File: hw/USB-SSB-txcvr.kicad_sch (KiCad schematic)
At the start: 0 parts

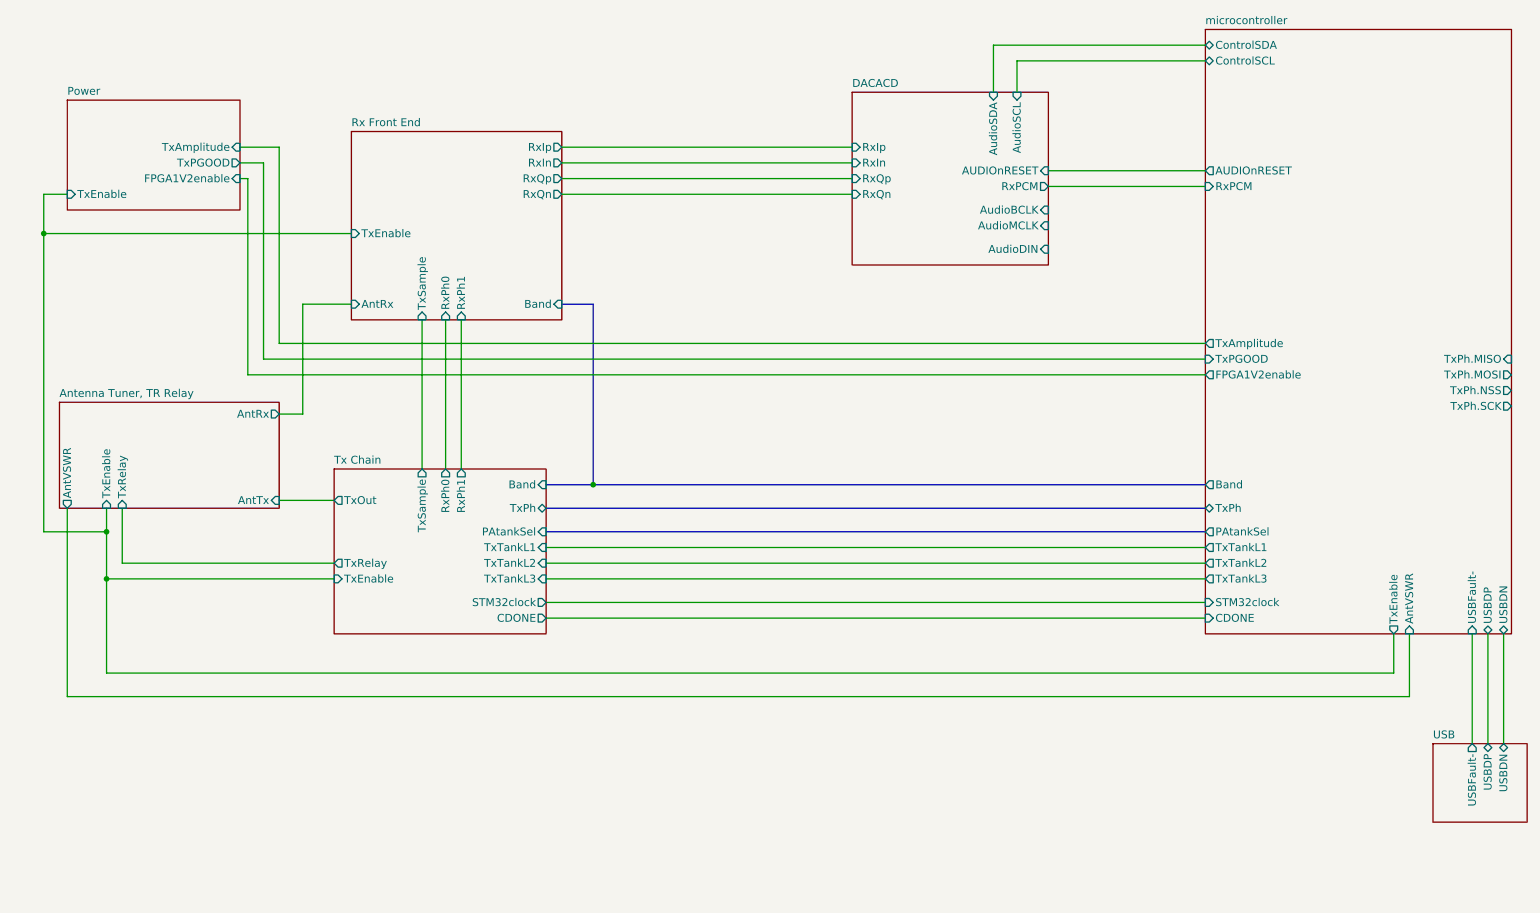
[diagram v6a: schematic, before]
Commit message: Embarking on a whole new arch for rx without BPFs and using a single digitally tuned tank plus three QSDs to accomplish image rejection in digital domain
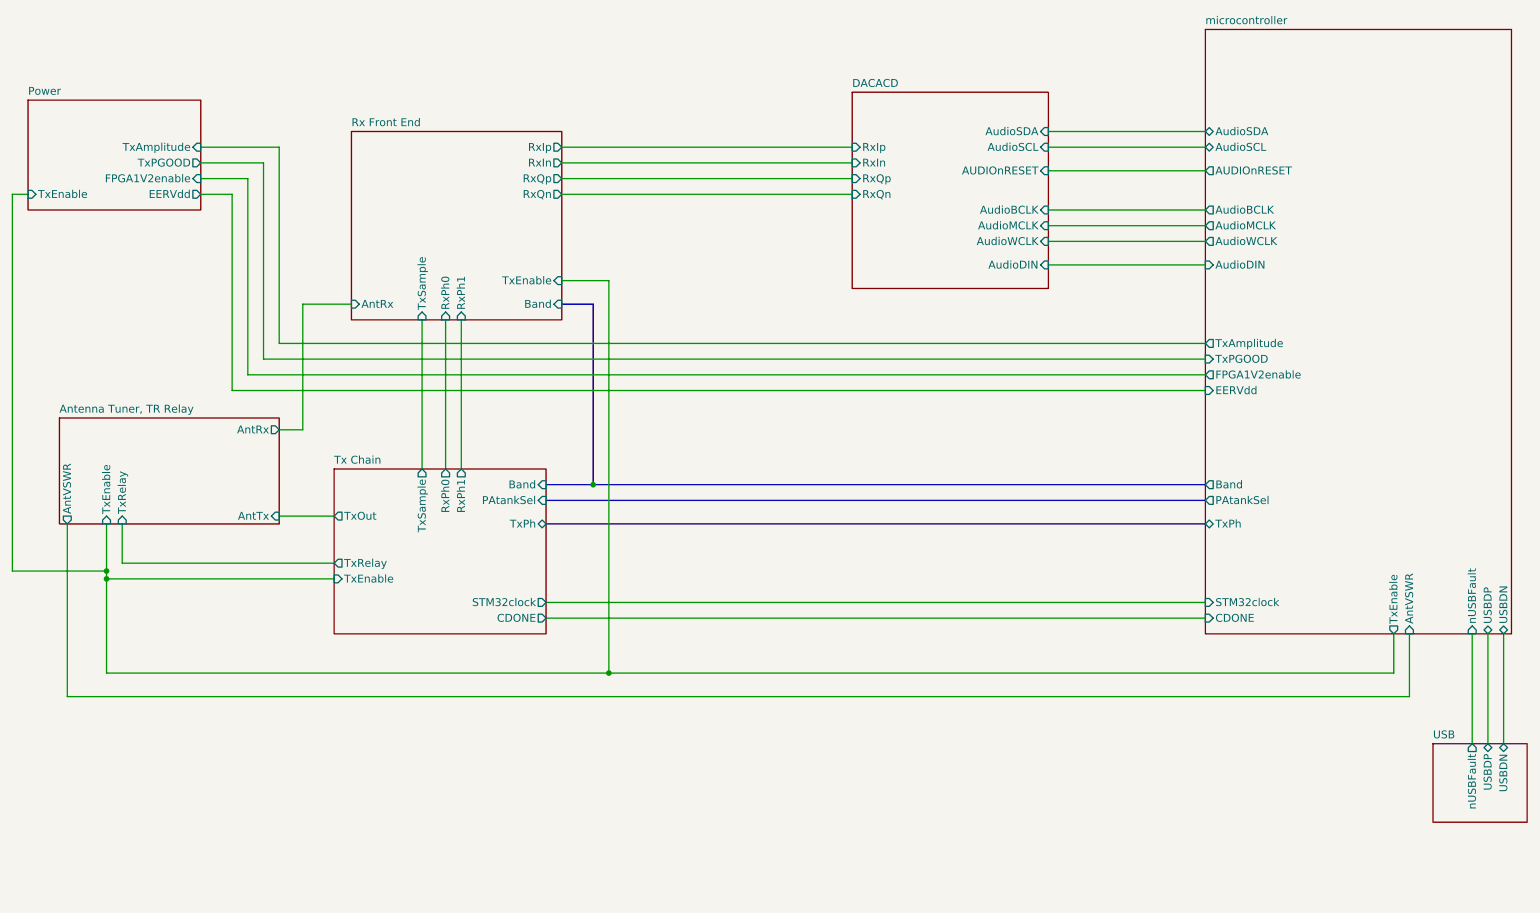
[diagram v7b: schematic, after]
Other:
- sheet DACACD ports: added AudioWCLK; removed RxPCM
- sheet Power ports: added EERVdd; removed none
- sheet Tx Chain ports: added none; removed TxTankL1, TxTankL2, TxTankL3
- sheet USB ports: added nUSBFault; removed USBFault-
- sheet microcontroller ports: added AudioBCLK, AudioDIN, AudioMCLK, AudioSCL, AudioSDA, AudioWCLK, EERVdd, nUSBFault; removed ControlSCL, ControlSDA, RxPCM, TxPh.MISO, TxPh.MOSI, TxPh.NSS, TxPh.SCK, TxTankL1, TxTankL2, TxTankL3, USBFault-

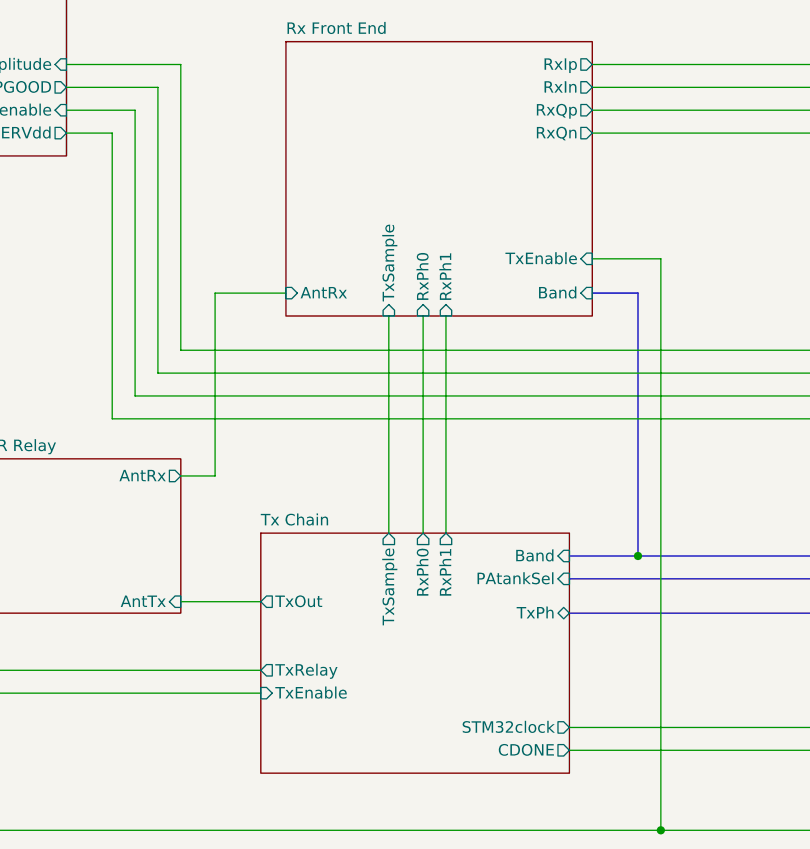
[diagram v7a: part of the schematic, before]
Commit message: Starting to switch to new rx architecture
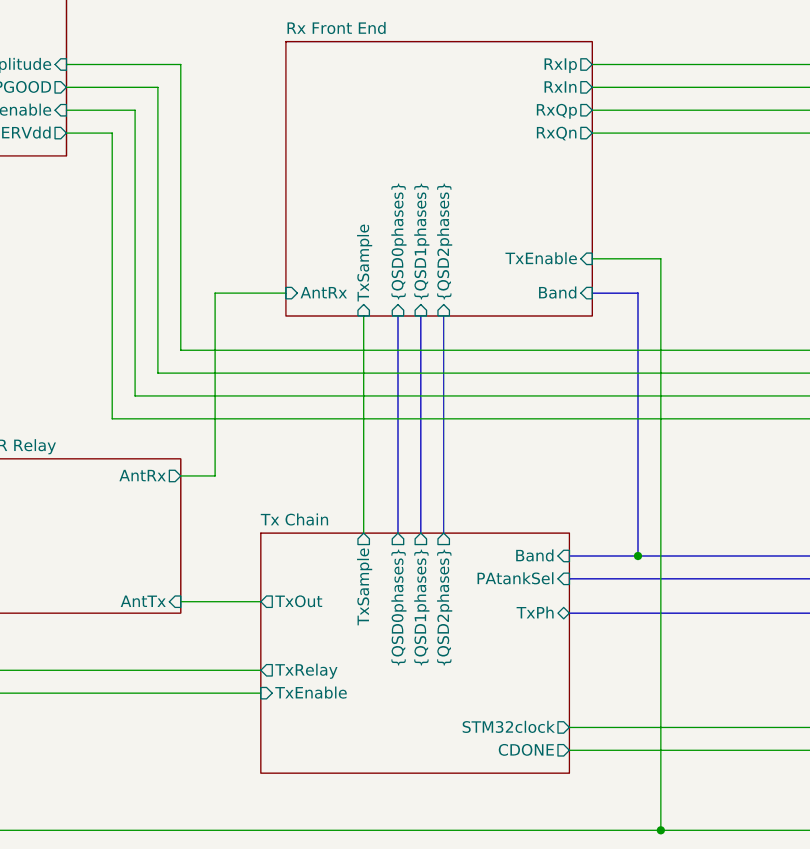
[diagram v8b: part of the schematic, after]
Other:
- sheet Rx Front End ports: added {QSD0phases}, {QSD1phases}, {QSD2phases}; removed RxPh0, RxPh1
- sheet Tx Chain ports: added {QSD0phases}, {QSD1phases}, {QSD2phases}; removed RxPh0, RxPh1
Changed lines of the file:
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@@
+		)
+	)
+	(bus
+		(pts
+			(xy 82.55 69.85) (xy 82.55 93.98)
+		)
+		(stroke
+			(width 0)
+			(type default)
 		)
 	)
@@
 	(bus
 		(pts
+			(xy 87.63 69.85) (xy 87.63 93.98)
+		)
+		(stroke
+			(width 0)
+			(type default)
+		)
+	)
+	(bus
+		(pts
 			(xy 109.22 96.52) (xy 208.28 96.52)
 		)
@@
 	(wire
 		(pts
-			(xy 81.534 69.85) (xy 81.534 93.98)
+			(xy 78.74 69.85) (xy 78.74 93.98)
 		)
 		(stroke
@@
 		)
 	)
-	(wire
-		(pts
-			(xy 87.884 93.98) (xy 87.884 69.85)
+	(bus
+		(pts
+			(xy 85.09 69.85) (xy 85.09 93.98)
 		)
 		(stroke
@@
 		(pts
 			(xy 104.14 44.45) (xy 151.13 44.45)
-		)
-		(stroke
-			(width 0)
-			(type default)
-		)
-	)
-	(wire
-		(pts
-			(xy 85.344 69.85) (xy 85.344 93.98)
 		)
 		(stroke
@@
 			)
 		)
-		(pin "RxPh0" input
-			(at 85.344 69.85 270)
-			(effects
-				(font
-					(size 1.27 1.27)
-				)
-				(justify left)
-			)
-		)
-		(pin "RxPh1" input
-			(at 87.884 69.85 270)
-			(effects
-				(font
-					(size 1.27 1.27)
-				)
-				(justify left)
-			)
-		)
 		(pin "TxSample" input
-			(at 81.534 69.85 270)
+			(at 78.74 69.85 270)
 			(effects
 				(font
@@
 				)
 				(justify right)
+			)
+		)
+		(pin "{QSD0phases}" input
+			(at 82.55 69.85 270)
+			(effects
+				(font
+					(size 1.27 1.27)
+				)
+				(justify left)
+			)
+		)
+		(pin "{QSD1phases}" input
+			(at 85.09 69.85 270)
+			(effects
+				(font
+					(size 1.27 1.27)
+				)
+				(justify left)
+			)
+		)
+		(pin "{QSD2phases}" input
+			(at 87.63 69.85 270)
+			(effects
+				(font
+					(size 1.27 1.27)
+				)
+				(justify left)
 			)
 		)
@@
 		)
 		(pin "TxSample" output
-			(at 81.534 93.98 90)
-			(effects
-				(font
-					(size 1.27 1.27)
-				)
-				(justify right)
-			)
-		)
-		(pin "RxPh0" output
-			(at 85.344 93.98 90)
-			(effects
-				(font
-					(size 1.27 1.27)
-				)
-				(justify right)
-			)
-		)
-		(pin "RxPh1" output
-			(at 87.884 93.98 90)
+			(at 78.74 93.98 90)
 			(effects
 				(font
@@
 			(effects
 				(font
+					(size 1.27 1.27)
+				)
+				(justify right)
+			)
+		)
+		(pin "{QSD0phases}" output
+			(at 82.55 93.98 90)
+			(effects
+				(font
+					(size 1.27 1.27)
+				)
+				(justify right)
+			)
+		)
+		(pin "{QSD1phases}" output
+			(at 85.09 93.98 90)
+			(effects
+				(font
+					(size 1.27 1.27)
+				)
+				(justify right)
+			)
+		)
+		(pin "{QSD2phases}" output
+			(at 87.63 93.98 90)
+			(effects
+				(font
